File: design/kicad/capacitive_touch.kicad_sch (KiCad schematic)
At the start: 31 parts, among them J10 Conn_01x09_Pin, J2 Conn_01x09_Pin, J4 Conn_01x09_Socket, J5 Conn_01x09_Socket, J6 Conn_01x09_Socket, J7 Conn_01x09_Socket, J8 Conn_01x09_Pin, J9 Conn_01x09_Pin, U4 MPR121QR2

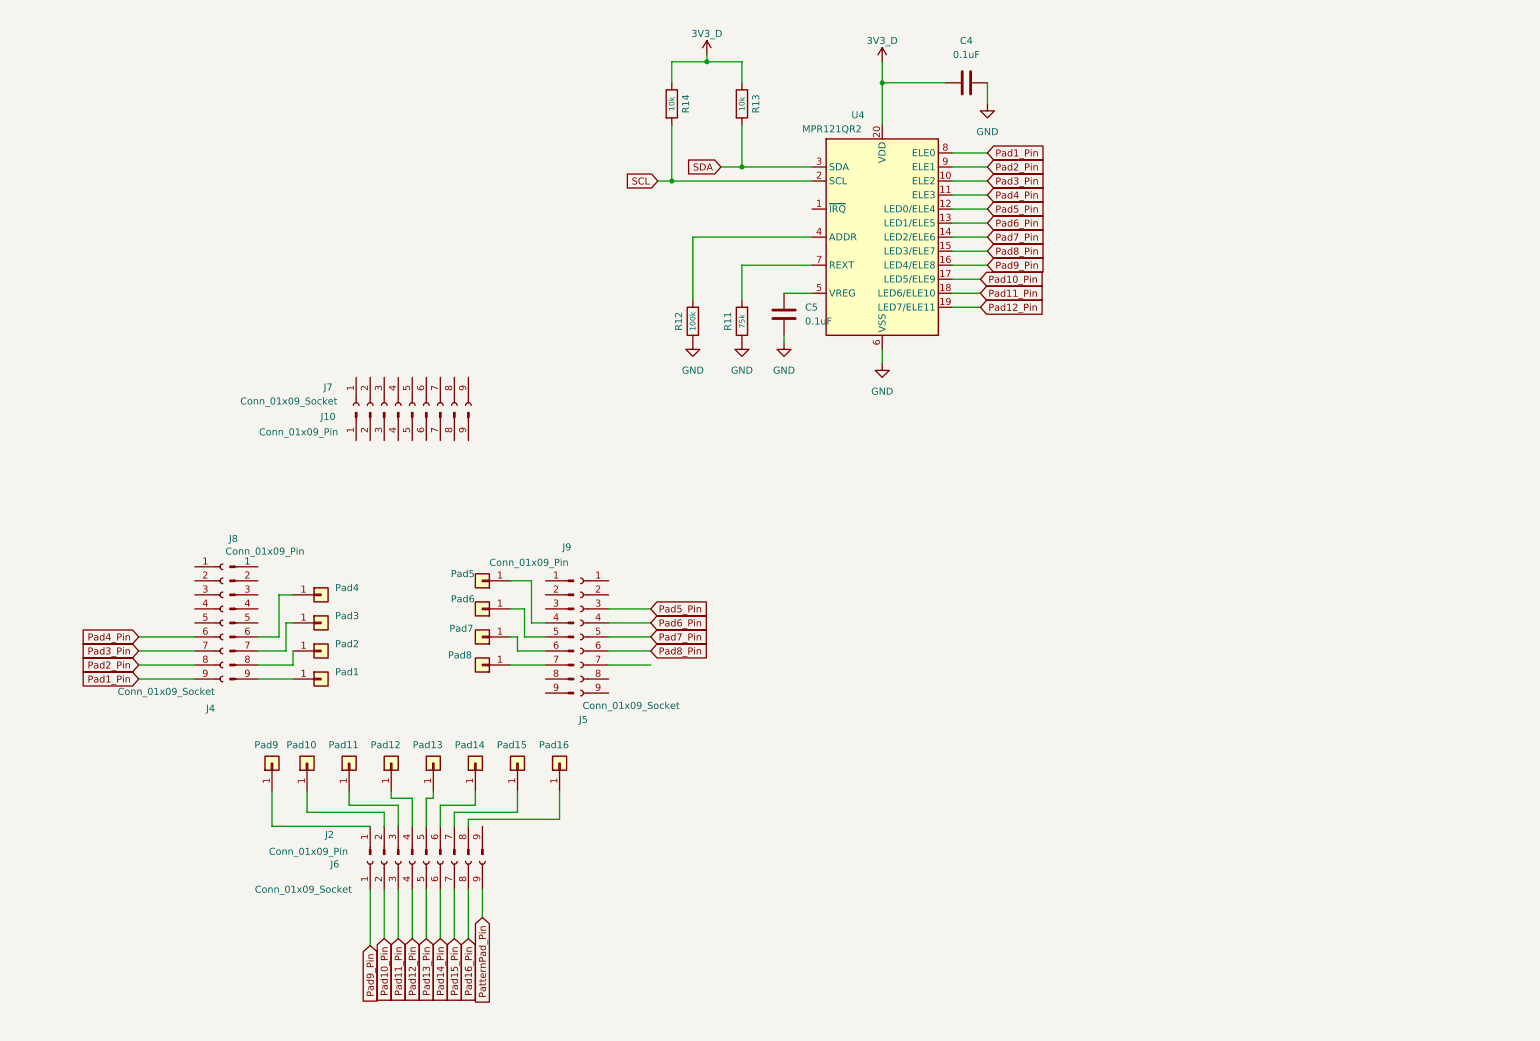
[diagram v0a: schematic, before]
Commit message: Completes all capacitive touch schematic work
3x capacitive touch ics and routing to pins
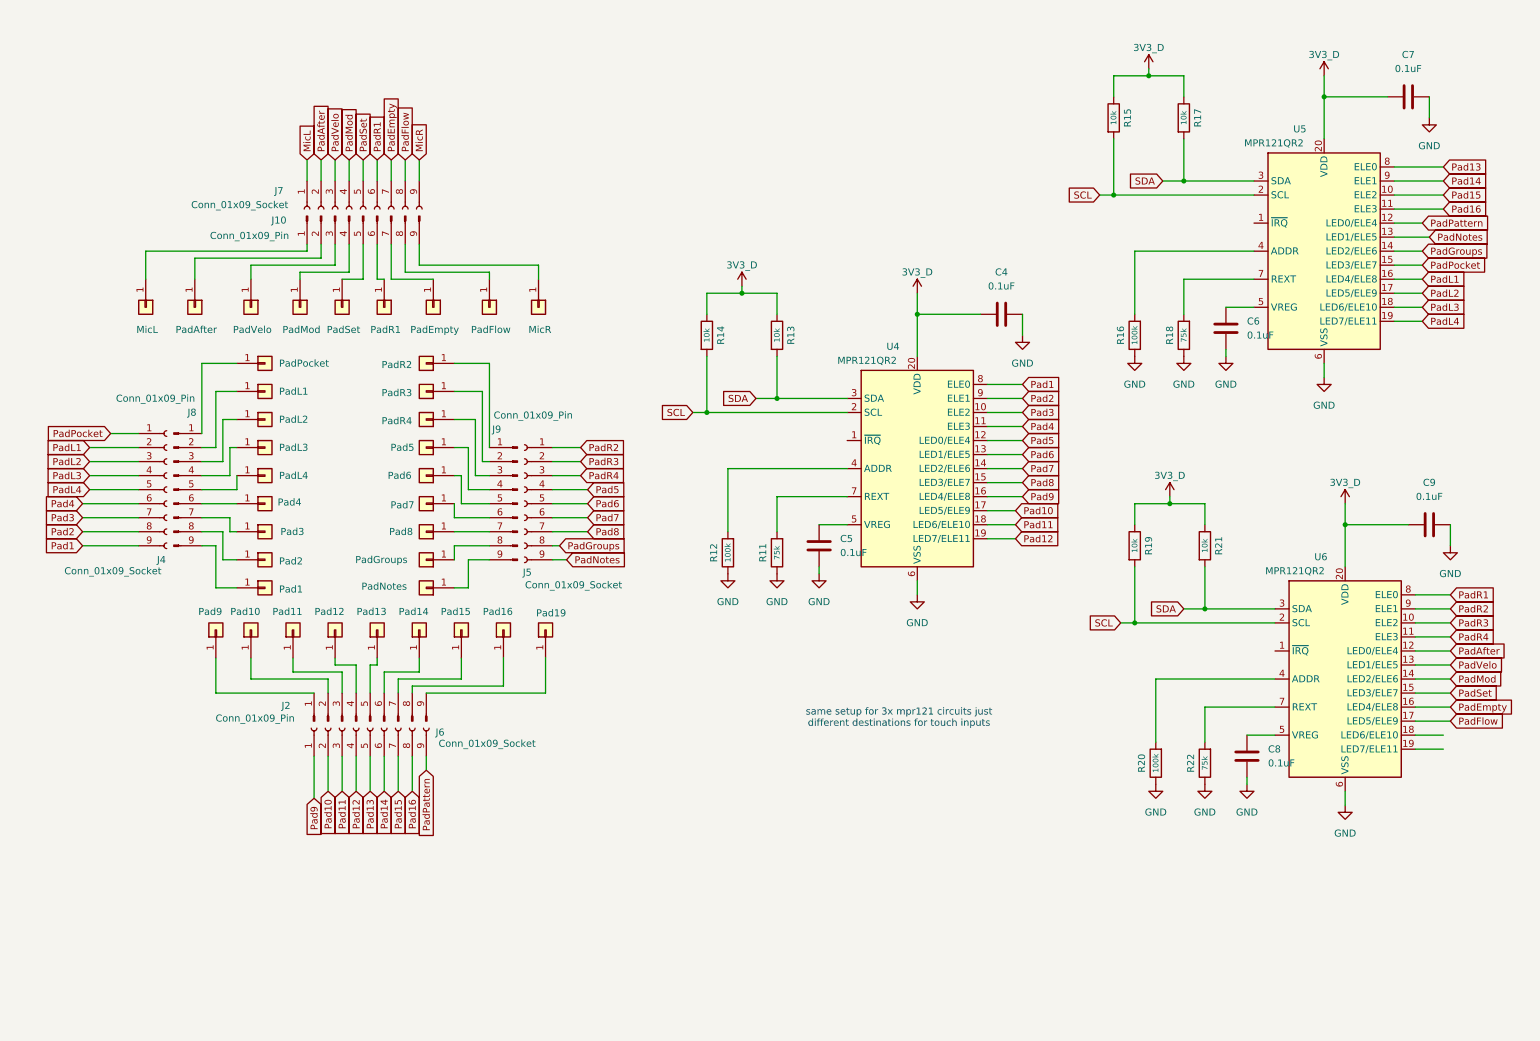
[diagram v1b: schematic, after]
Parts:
- added C6, C7, C8, C9: 0.1uF, Capacitor_SMD:C_0603_1608Metric, symbol Device:C
- added MicL, MicR, Pad19, PadAfter, PadEmpty, PadFlow, PadGroups, PadL1, PadL2, PadL3, PadL4, PadMod, PadNotes, PadPocket, PadR1, PadR2, PadR3, PadR4, PadSet, PadVelo: Conn_01x01, symbol Connector_Generic:Conn_01x01
- added R15, R17, R19, R21: 10k, Resistor_SMD:R_0603_1608Metric, symbol Device:R
- added R16, R20: 100k, Resistor_SMD:R_0603_1608Metric, symbol Device:R
- added R18, R22: 75k, Resistor_SMD:R_0603_1608Metric, symbol Device:R
- added U5, U6: MPR121QR2, Package_DFN_QFN:UQFN-20_3x3mm_P0.4mm, symbol Sensor_Touch:MPR121QR2
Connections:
- net 3V3_D: now also C7.2, C9.2, R15.1, R17.1, R19.1, R21.1, U5.20 (VDD), U6.20 (VDD)
- net GND: now also C6.1, C7.1, C8.1, C9.1, R16.1, R18.1, R20.1, R22.1, U5.6 (VSS), U6.6 (VSS)
- net SCL: now also R15.2, R19.2, U5.2 (SCL), U6.2 (SCL)
- net SDA: now also R17.2, R21.2, U5.3 (SDA), U6.3 (SDA)
- net MicL: now reaches J7.1 (Pin_1)
- net PadAfter: now reaches J7.2 (Pin_2)
- net PadAfter: now also U6.12 (LED0/ELE4)
- net PadVelo: now reaches J7.3 (Pin_3)
- net PadVelo: now also U6.13 (LED1/ELE5)
- net PadMod: now reaches J7.4 (Pin_4)
- net PadMod: now also U6.14 (LED2/ELE6)
- net PadSet: now reaches J7.5 (Pin_5)
- net PadSet: now also U6.15 (LED3/ELE7)
- net PadR1: now reaches J7.6 (Pin_6)
- net PadR1: now also U6.8 (ELE0)
- net PadEmpty: now reaches J7.7 (Pin_7)
- net PadEmpty: now also U6.16 (LED4/ELE8)
- net PadFlow: now reaches J7.8 (Pin_8)
- net PadFlow: now also U6.17 (LED5/ELE9)
- net MicR: now reaches J7.9 (Pin_9)
- net at J2.9 (Pin_9): now also Pad19.1 (Pin_1)
- net at J9.1 (Pin_1): now also PadR2.1 (Pin_1)
- net at J9.2 (Pin_2): now also PadR3.1 (Pin_1)
- net at J9.3 (Pin_3): now also PadR4.1 (Pin_1)
- net at J9.8 (Pin_8): now also PadGroups.1 (Pin_1)
- net at J9.9 (Pin_9): now also PadNotes.1 (Pin_1)
- net PadPocket: now reaches J4.1 (Pin_1)
- net PadPocket: now also U5.15 (LED3/ELE7)
- net PadL1: now reaches J4.2 (Pin_2)
- net PadL1: now also U5.16 (LED4/ELE8)
- net PadL2: now reaches J4.3 (Pin_3)
- net PadL2: now also U5.17 (LED5/ELE9)
- net PadL3: now reaches J4.4 (Pin_4)
- net PadL3: now also U5.18 (LED6/ELE10)
- net PadL4: now reaches J4.5 (Pin_5)
- net PadL4: now also U5.19 (LED7/ELE11)
- net at J8.1 (Pin_1): now also PadPocket.1 (Pin_1)
- net at J8.2 (Pin_2): now also PadL1.1 (Pin_1)
- net at J8.3 (Pin_3): now also PadL2.1 (Pin_1)
- net at J8.4 (Pin_4): now also PadL3.1 (Pin_1)
- net at J8.5 (Pin_5): now also PadL4.1 (Pin_1)
- net at J10.1 (Pin_1): now also MicL.1 (Pin_1)
- net at J10.2 (Pin_2): now also PadAfter.1 (Pin_1)
- net at J10.3 (Pin_3): now also PadVelo.1 (Pin_1)
- net at J10.4 (Pin_4): now also PadMod.1 (Pin_1)
- net at J10.5 (Pin_5): now also PadSet.1 (Pin_1)
- net at J10.6 (Pin_6): now also PadR1.1 (Pin_1)
- net at J10.7 (Pin_7): now also PadEmpty.1 (Pin_1)
- net at J10.8 (Pin_8): now also PadFlow.1 (Pin_1)
- net at J10.9 (Pin_9): now also MicR.1 (Pin_1)
- net PadR2: now reaches J5.1 (Pin_1)
- net PadR2: now also U6.9 (ELE1)
- net PadR3: now reaches J5.2 (Pin_2)
- net PadR3: now also U6.10 (ELE2)
- net Pad8: now reaches J5.7 (Pin_7)
- net Pad8: now also U4.15 (LED3/ELE7)
- net PadGroups: now reaches J5.8 (Pin_8)
- net PadGroups: now also U5.14 (LED2/ELE6)
- net PadNotes: now reaches J5.9 (Pin_9)
- net PadNotes: now also U5.13 (LED1/ELE5)
- net Pad10_Pin renamed Pad10
- net Pad11_Pin renamed Pad11
- net Pad12_Pin renamed Pad12
- net Pad13_Pin renamed Pad13
- net Pad13: now also U5.8 (ELE0)
- net Pad14_Pin renamed Pad14
- net Pad14: now also U5.9 (ELE1)
- net Pad15_Pin renamed Pad15
- net Pad15: now also U5.10 (ELE2)
- net Pad16_Pin renamed Pad16
- net Pad16: now also U5.11 (ELE3)
- net Pad1_Pin renamed Pad1
- net Pad2_Pin renamed Pad2
- net Pad3_Pin renamed Pad3
- net Pad4_Pin renamed Pad4
- net Pad5_Pin renamed Pad5
- net Pad5: now also J5.4 (Pin_4); no longer J5.3 (Pin_3)
- net Pad6_Pin renamed Pad6
- net Pad6: now also J5.5 (Pin_5); no longer J5.4 (Pin_4)
- net Pad7_Pin renamed Pad7
- net Pad7: now also J5.6 (Pin_6); no longer J5.5 (Pin_5)
- removed net Pad8_Pin: J5.6 (Pin_6), U4.15 (LED3/ELE7)
- net Pad9_Pin renamed Pad9
- net PatternPad_Pin renamed PadPattern
- net PadPattern: now also U5.12 (LED0/ELE4)
- new net: R16.2, U5.4 (ADDR)
- new net: C6.2, U5.5 (VREG)
- new net: R18.2, U5.7 (REXT)
- new net: R20.2, U6.4 (ADDR)
- new net: C8.2, U6.5 (VREG)
- new net: R22.2, U6.7 (REXT)
- new net PadR4: J5.3 (Pin_3), U6.11 (ELE3)
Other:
- note added: "same setup for 3x mpr121 circuits just different destinations for touch inputs"
- moved on the sheet: C4, C5, J10, J2, J4, J5, J6, J7, J8, J9, Pad1, Pad10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

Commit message: adds LEDs to design schematic
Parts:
- R11, R12, R16, R20: LCSC (none) -> C2907088
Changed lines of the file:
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@@
 			)
 		)
+		(property "LCSC" " C2907088"
+			(at 137.16 111.76 90)
+			(effects
+				(font
+					(size 1.27 1.27)
+				)
+				(hide yes)
+			)
+		)
 		(pin "2"
 		)
@@
 			)
 		)
+		(property "LCSC" " C2907088"
+			(at 214.63 149.86 0)
+			(effects
+				(font
+					(size 1.27 1.27)
+				)
+				(hide yes)
+			)
+		)
 		(pin "2"
 		)
@@
 			)
 		)
+		(property "LCSC" " C2907088"
+			(at 146.05 111.76 90)
+			(effects
+				(font
+					(size 1.27 1.27)
+				)
+				(hide yes)
+			)
+		)
 		(pin "2"
 		)
@@
 			(at 210.82 72.39 0)
 			(effects
+				(font
+					(size 1.27 1.27)
+				)
+				(hide yes)
+			)
+		)
+		(property "LCSC" " C2907088"
+			(at 210.82 72.39 0)
+			(effects
